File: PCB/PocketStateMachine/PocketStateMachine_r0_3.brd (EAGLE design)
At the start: 42.2 x 52.8 mm, 10 parts, among them IC1 SN65HVD31DR

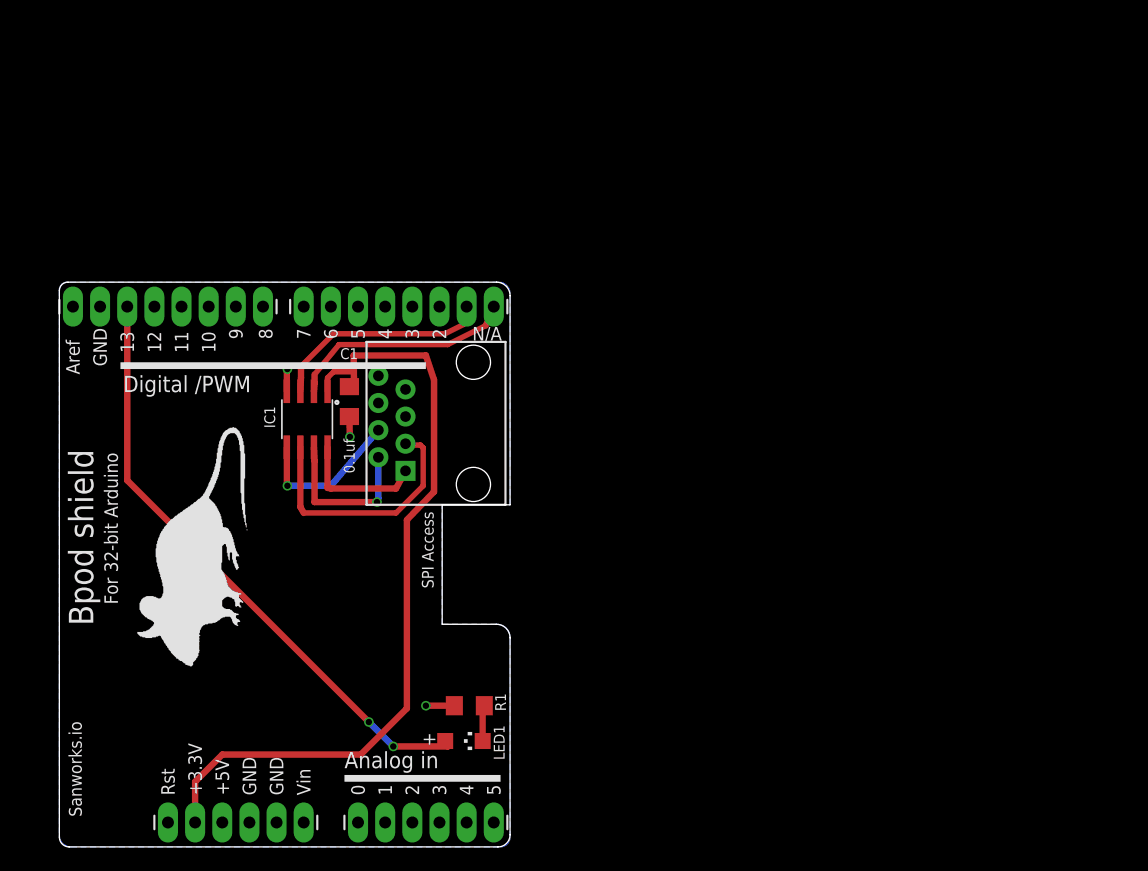
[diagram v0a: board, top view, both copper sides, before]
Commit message: -Added design files for the Pocket State Machine - a new state machine module with many improvements, based on Teensy 3.6. -Added design files for isolated valve driver module -Added new revision of Bpod arduino shield, allowing modules to be powered from the Pocket State Machine (when they do not require a USB connection)
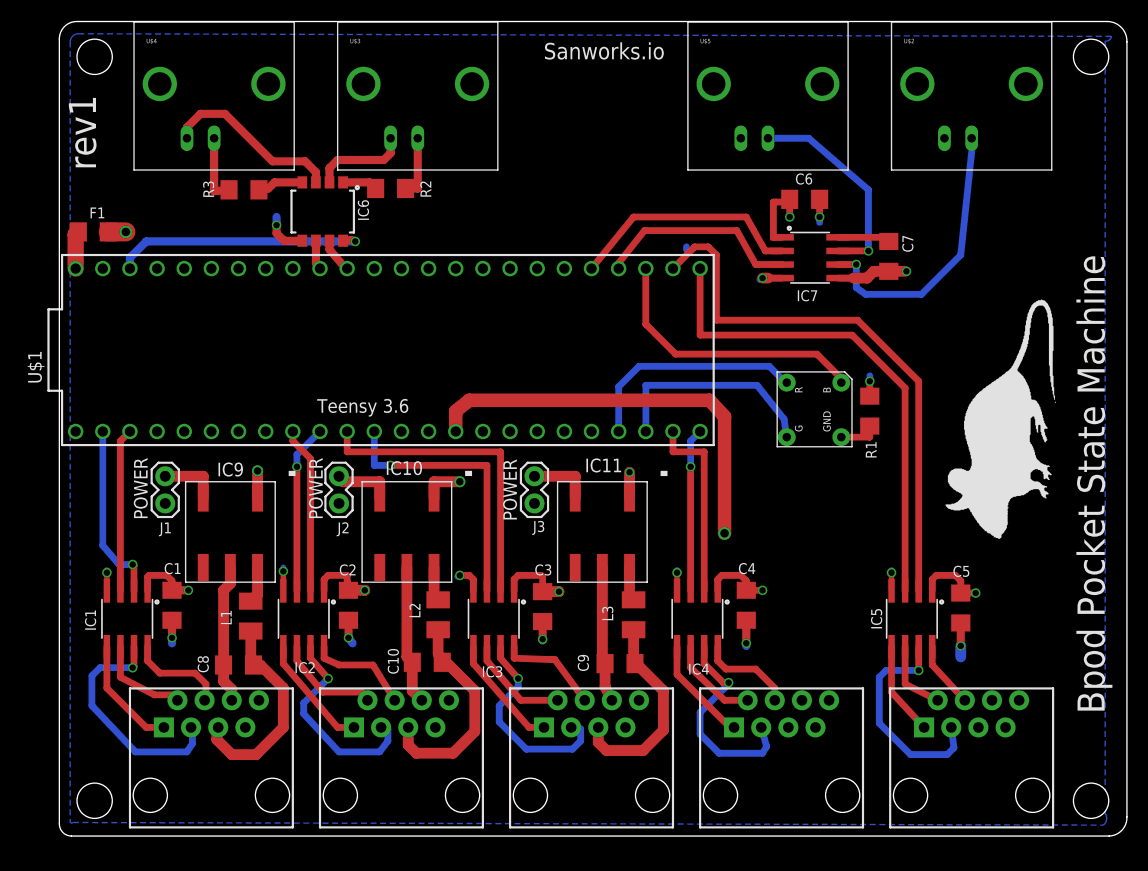
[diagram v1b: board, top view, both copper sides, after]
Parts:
- removed ALG, PWR: (no value), SparkFun:1X06_LONGPADS
- removed DIGI1, DIGI2: (no value), SparkFun:1X08_LONGPADS
- removed LED1: (no value), adafruit:CHIPLED_1206
- added C10, C8, C9: 2.2uf, SparkFun-Capacitors:1206
- added C2, C3, C4, C5, C6, C7: 0.1uf, SparkFun-Capacitors:1206
- added F1: 6V/0.5A, SparkFun-Fuses:1206
- added IC10, IC11, IC9: MTU1D0505MC, JoshParts10:MTU1D0505MC
- added IC2, IC3, IC4, IC5: SN65HVD31DR, Joshparts4:SO08
- added IC6: OPTOISOLATOR-2SOIC8, SparkFun-DiscreteSemi:SO08-2
- added IC7: ADUM5240, SparkFun-DigitalIC:SO08
- added J1, J2, J3: (no value), SparkFun-Connectors:1X02
- added JP1, JP3, JP4, JP5: STAND-OFF, SparkFun:STAND-OFF
- added L1, L2, L3: (no value), rcl:L3225M
- added R2, R3: 220, SparkFun-Resistors:1206
- added SERIAL1, SERIAL2, SERIAL3, SERIAL4, SERIAL5: RJ45-8PTH, SparkFun:RJ45-8
- added U$3, U$4, U$5: BNCPTH, SparkFun:BNC
- added U$8: SQUARE_TRICOLOR_LED, JoshParts:SQUARE_TRICOLOR_LED
- added U$9: (no value), JoshParts:MOUSELOGO
- C1: value (none) -> 0.1uf
- R1: value 56 -> 47; device SparkFun-Resistors:1206 -> SparkFun-Passives:1206
- U$1: value RJ45-8PTH -> TEENSY_3.6_DIL; device SparkFun:RJ45-8 -> Teensy_3_and_LC_Series_Boards_v1.4:TEENSY_3.6_DIL
- U$2: value (none) -> BNCPTH; device JoshParts:MOUSELOGO -> SparkFun:BNC
- moved U$2 95.0 mm to (85.3, 65.3)
- moved R1 46.5 mm to (75.8, 39.8), turned to 270 degrees
- moved C1 25.3 mm to (10.5, 21.6)
- moved IC1 25.1 mm to (6.35, 20.3)
- moved U$1 11.5 mm to (29.5, 45.5)
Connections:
- new net 5V: C6.2, F1.2, IC10.+VIN, IC11.+VIN, IC7.1, IC9.+VIN
- new net BNCIN1: IC6.7, U$1.16/A2
- new net BNCIN2: IC6.6, U$1.17/A3
- new net ISOGND: C7.1, IC7.5, U$2.GND, U$5.GND
- new net LED_BLUE: U$1.35/A16, U$8.P$3
- new net LED_GREEN: U$1.30, U$8.P$1
- new net LED_RED: U$1.29, U$8.P$4
- new net N$11: IC1.2, U$1.0
- new net N$12: IC1.3, U$1.1
- new net N$13: IC6.3, U$4.GND
- new net N$14: R3.2, U$4.S
- new net N$15: R2.2, U$3.S
- new net N$16: IC6.2, U$3.GND
- new net N$17: IC2.8, SERIAL3.4
- new net N$18: IC2.7, SERIAL3.3
- new net N$19: IC2.6, SERIAL3.2
- new net N$20: IC7.3, U$1.36/A17
- new net N$21: IC2.5, SERIAL3.1
- new net N$22: IC2.2, U$1.7
- new net N$23: C8.2, L1.2, SERIAL5.5
- new net N$24: IC7.2, U$1.37/A18
- new net N$25: R1.2, U$8.P$2
- new net N$26: C8.1, IC9.0V, SERIAL5.6
- new net N$27: IC7.7, U$5.S
- new net N$28: IC2.3, U$1.8
- new net N$29: F1.1, U$1.VIN
- new net N$30: IC7.6, U$2.S
- new net N$32: IC5.8, SERIAL1.4
- new net N$33: IC5.7, SERIAL1.3
- new net N$34: IC5.6, SERIAL1.2
- new net N$35: IC5.5, SERIAL1.1
- new net N$36: IC4.8, SERIAL2.4
- new net N$37: IC4.7, SERIAL2.3
- new net N$38: IC4.6, SERIAL2.2
- new net N$39: IC9.+VOUT, L1.1
- new net N$40: IC4.5, SERIAL2.1
- new net N$41: IC9.-VIN, J1.2
- new net N$42: IC5.2, U$1.34/A15
- new net N$43: C10.1, IC10.0V, SERIAL3.6
- new net N$44: C10.2, L2.2, SERIAL3.5
- new net N$45: IC10.+VOUT, L2.1
- new net N$46: IC10.-VIN, J2.2
- new net N$47: C9.1, IC11.0V, SERIAL4.6
- new net N$48: IC5.3, U$1.33/A14
- new net N$49: C9.2, L3.2, SERIAL4.5
- new net N$5: IC3.2, U$1.9
- new net N$50: IC11.+VOUT, L3.1
- new net N$51: IC11.-VIN, J3.2
- new net N$52: IC4.2, U$1.31/A12
- new net N$53: IC4.3, U$1.32/A13
- new net N$54: IC6.1, R2.1
- new net N$55: IC6.4, R3.1
- new net N$64: C7.2, IC7.8
- new net VCC: C1.1, C2.1, C3.1, C4.1, C5.1, IC1.1, IC2.1, IC3.1, IC4.1, IC5.1, IC6.8, U$1.3.3V, U$1.3.3V3
- net GND: now also C2.2, C3.2, C4.2, C5.2, C6.1, IC2.4, IC3.4, IC4.4, IC5.4, IC6.5, IC7.4, J1.1, J2.1, J3.1, U$1.AGND, U$1.GND, U$1.GND1; no longer PWR.4, PWR.5
- net N$1: now also IC3.8, SERIAL4.4; no longer C1.1, IC1.1, PWR.2
- net N$10: now also SERIAL5.1; no longer U$1.4
- net N$2: now also IC3.7, SERIAL4.3; no longer LED1.C, R1.2
- net N$3: now also IC3.6, SERIAL4.2; no longer DIGI2.3, LED1.A
- net N$4: now also IC3.5, SERIAL4.1; no longer DIGI1.7, IC1.3
- net N$6: now also IC3.3, U$1.10; no longer DIGI1.8, IC1.2
- net N$7: now also SERIAL5.4; no longer U$1.1
- net N$8: now also SERIAL5.3; no longer U$1.2
- net N$9: now also SERIAL5.2; no longer U$1.3
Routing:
- net VCC: track 0.00 -> 100.2 mm, vias 0 -> 7
- net N$1: track 77.3 -> 9.60 mm
- net N$42: track 0.00 -> 52.2 mm
- net N$3: track 57.1 -> 9.61 mm, vias 2 -> 0
- net N$48: track 0.00 -> 46.4 mm
- net N$5: track 0.00 -> 29.3 mm
- net GND: track 7.02 -> 33.6 mm, vias 3 -> 14
- net N$30: track 0.00 -> 26.4 mm, vias 0 -> 1
- net LED_BLUE: track 0.00 -> 26.0 mm
- net N$24: track 0.00 -> 22.0 mm
- net LED_RED: track 0.00 -> 21.3 mm
- net 5V: track 0.00 -> 21.1 mm, vias 0 -> 5
- net N$33: track 0.00 -> 20.9 mm, vias 0 -> 1
- net LED_GREEN: track 0.00 -> 20.5 mm
- net N$44: track 0.00 -> 20.4 mm
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- added copper zone on layer 2, net 5V
- added copper zone on layer 15, net GND
- added copper zone on layer 15, net ISOGND
- added copper zone on layer 2, net VCC
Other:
- board size 42.2 x 52.8 mm -> 99.9 x 76.2 mm
- board text added: "Bpod Pocket State Machine"
- board text added: "POWER"
- board text added: "Teensy 3.6"
- board text added: "rev1"
- board text removed: "+"
- board text removed: "+3.3V"
- board text removed: "+5V"
- board text removed: "0"
- board text removed: "0.1uf"
- board text removed: "1"
- board text removed: "10"
- board text removed: "11"
- board text removed: "12"
- board text removed: "13"
- board text removed: "2"
- board text removed: "3"
- board text removed: "4"
- board text removed: "5"
- board text removed: "6"
- board text removed: "7"
- board text removed: "8"
- board text removed: "9"
- board text removed: "Analog in"
- board text removed: "Aref"
- board text removed: "Bpod shield"
- board text removed: "Digital /PWM"
- board text removed: "For 32-bit Arduino"
- board text removed: "GND"
- board text removed: "N/A"
- board text removed: "Rst"
- board text removed: "SPI Access"
- board text removed: "Vin"
